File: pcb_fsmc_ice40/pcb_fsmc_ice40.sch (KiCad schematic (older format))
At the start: 40 parts, among them P2 CONN_01X20, P3 CONN_01X20, P4 MICRO-SD, P5 CONN_01X12, P6 CONN_01X12, P7 KNUSB, U1 STM32F40X_LQFP144, X1 CRYSTAL

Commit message: Some more work on PCB, still work left to do.
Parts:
- added C1: 10uF, Capacitors_SMD:C_0805, symbol C_Small
- added JP1: Jumper_NO_Small, Pin_Headers:Pin_Header_Straight_1x02, symbol Jumper_NO_Small
- added R4, R5: 47k, Resistors_SMD:R_0603, symbol R_Small
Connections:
- net labels added: boot0, boot1
- net labels removed: pb2
- wire segments 270 -> 278
- no-connect marks 1 -> 3
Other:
- note added: "Boot selection"
- note added: "Jumper off boots from flash (BOOT0=0)\nJumper on boots from system/DFU\n (BOOT0=1 BOOT1=0)"

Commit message: Mostly complete routing.
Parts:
- removed JP1: Jumper_NO_Small, Pin_Headers:Pin_Header_Straight_1x02, symbol Jumper_NO_Small
- removed P2, P3: CONN_01X20, knielsenlib:ice40_vert_conn, symbol CONN_01X20
- removed P4: MICRO-SD, knielsenlib:SD_502774, symbol MICRO-SD
- removed P5, P6: CONN_01X12, knielsenlib:ice40_top_conn_12, symbol CONN_01X12
- added P1: SD_CARD, knielsenlib:SD_CARD_10100, symbol SD_CARD
- added P2: CONN_02X20, knielsenlib:ice40_vert_conn, symbol CONN_02X20
- added P5: CONN_02X12, knielsenlib:ice40_top_conn_12, symbol CONN_02X12
- added SW1: SWITCH_INV, knielsenlib:switch_msk_12c02, symbol SWITCH_INV
- B1: footprint knielsenlib:SWITCH_FSMJSMA -> knielsenlib:pushbutton_EVQ_PSR02K
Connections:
- net labels added: pb3, pc13, pc14, pe0, pe1, pg12, pg15, user_led1, user_led2
- net labels removed: pa15, pa8, pa9, pb12, pb13, pg6, sram4_ce, sram_bhe, sram_ble, swo, user_led
- wire segments 278 -> 285
- no-connect marks 3 -> 57
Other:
- moved on the sheet: C1, C30, R3, R5, U1A

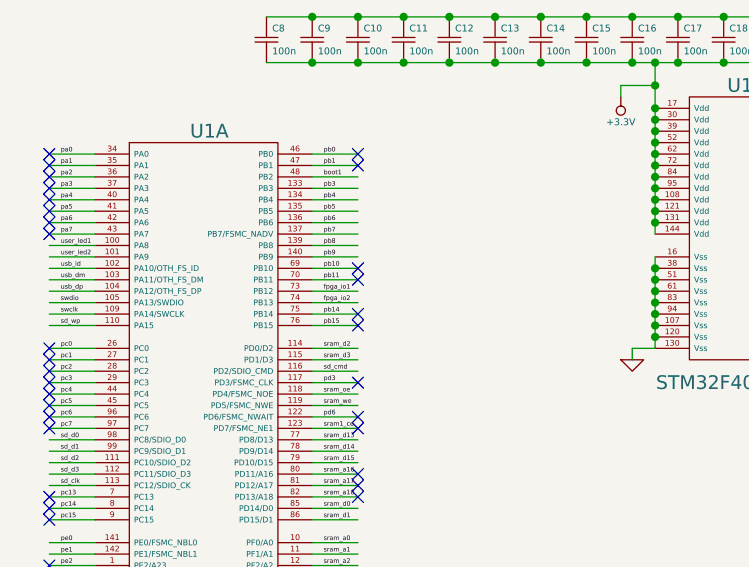
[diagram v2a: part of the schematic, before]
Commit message: Move the extra IO fpga_io1 and fpga_io2 to PB10/PB11.
These have USART Rx/Tx available, so we can use these two spare IOs
with the trick wher ethe FPGA proxies the UART signal from STM32 to
the FTDI chip on the ICE40 board, simplifying serial debugging.
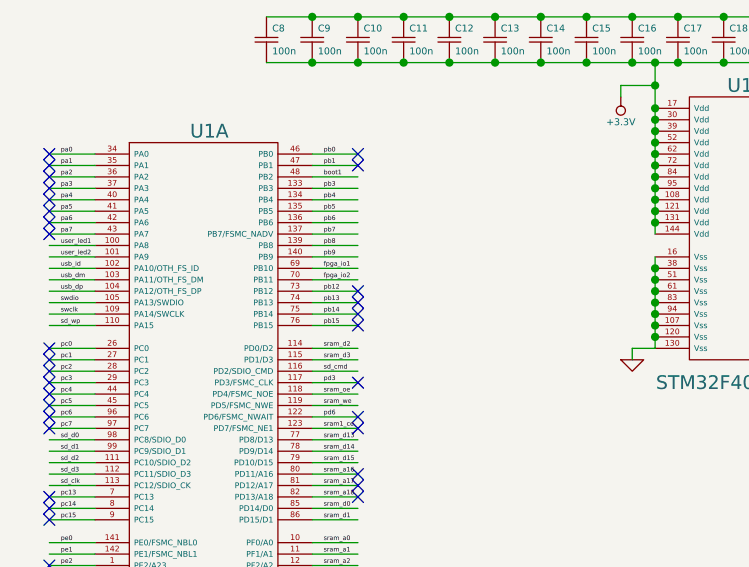
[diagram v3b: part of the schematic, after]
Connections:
- net labels added: pb12, pb13
- net labels removed: pb10, pb11
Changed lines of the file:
@@
 pb14
 Text Label 2100 1900 0    20   ~ 0
+pb13
+Text Label 2100 1850 0    20   ~ 0
+pb12
+Text Label 2100 1800 0    20   ~ 0
 fpga_io2
-Text Label 2100 1850 0    20   ~ 0
+Text Label 2100 1750 0    20   ~ 0
 fpga_io1
-Text Label 2100 1800 0    20   ~ 0
-pb11
-Text Label 2100 1750 0    20   ~ 0
-pb10
 Text Label 2100 1700 0    20   ~ 0
 pb9
@@
 NoConn ~ 2250 1250
 NoConn ~ 2250 1300
-NoConn ~ 2250 1750
-NoConn ~ 2250 1800
 NoConn ~ 2250 1950
 NoConn ~ 2250 2000
@@
 	-1   0    0    1
 $EndComp
+NoConn ~ 2250 1850
+NoConn ~ 2250 1900
 $EndSCHEMATC
